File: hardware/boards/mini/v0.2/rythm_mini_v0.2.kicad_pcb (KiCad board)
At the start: 8 copper layers, 18 x 50 mm, 80 parts, among them IC1 NAU88C22YG, IC2 IS42S32160F-6BLI, Q1 PMV37EN22, U1 W25Q128JVP, U2 LTV-217-G, U4 STM32H750XBHx, U5 MT48LC32M8A2TG, Y1 Crystal_GND24

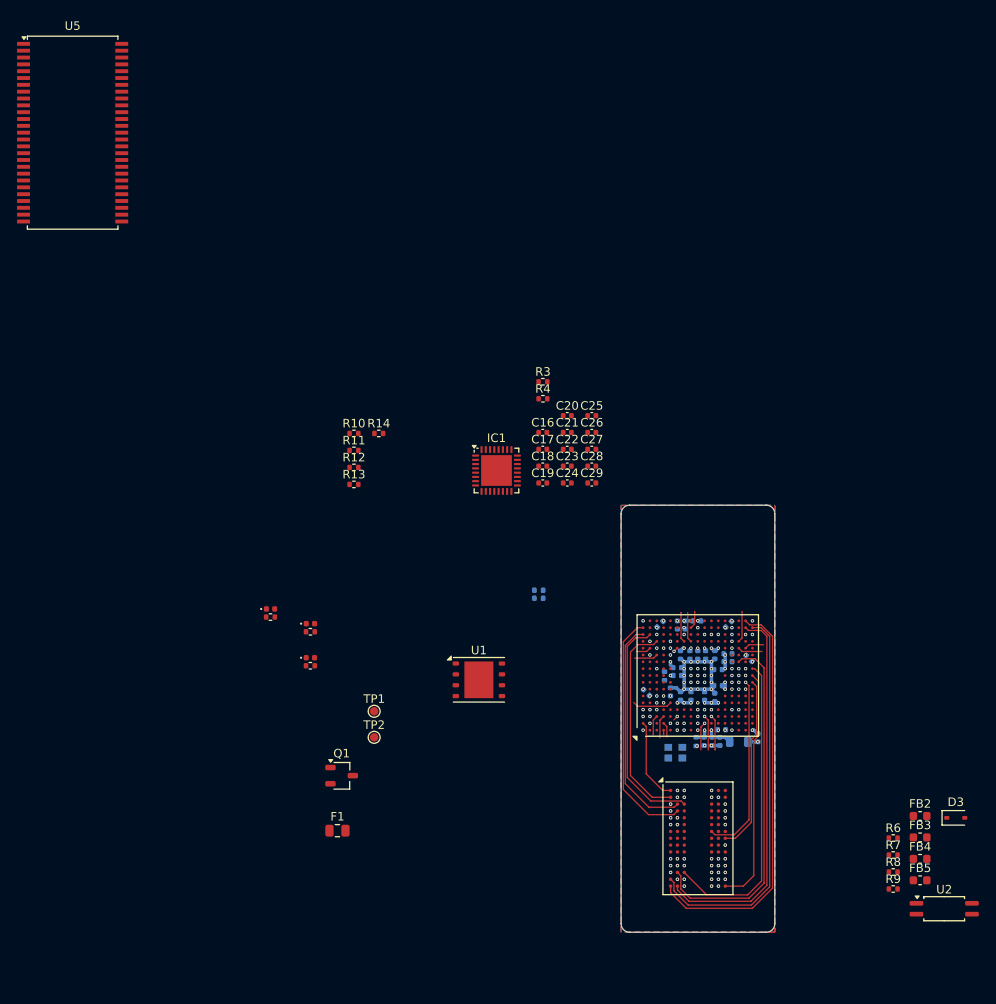
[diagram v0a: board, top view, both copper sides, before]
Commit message: minor module routing cleanup
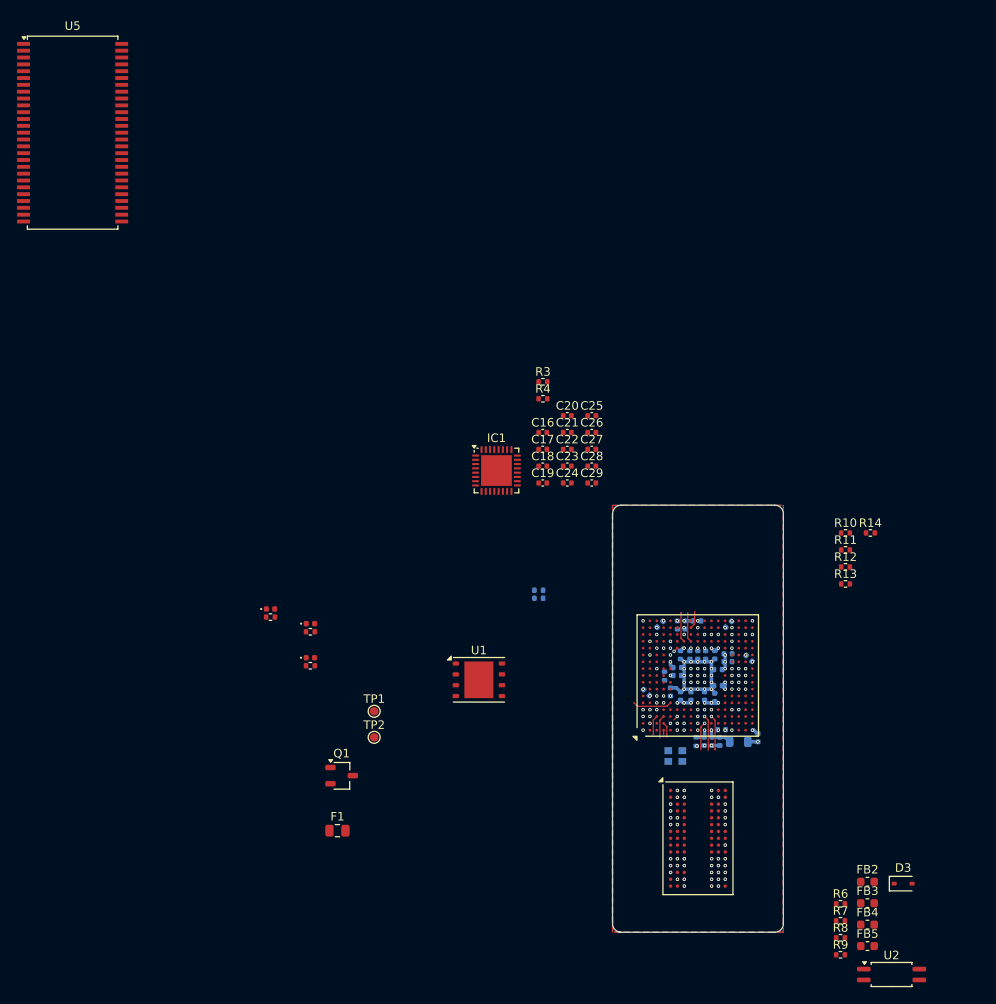
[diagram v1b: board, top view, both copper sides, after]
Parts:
- moved R10 58.7 mm to (97.3, 58.2)
- moved R11 58.7 mm to (97.3, 60.2)
- moved R12 58.7 mm to (97.3, 62.2)
- moved R13 58.7 mm to (97.3, 64.2)
- moved R14 58.7 mm to (100.2, 58.2)
- moved D3 9.86 mm to (104.0, 99.3)
- moved FB2 9.86 mm to (99.8, 99.1)
- moved FB4 9.86 mm to (99.8, 104.1)
- moved FB5 9.86 mm to (99.8, 106.6)
- moved R6 9.86 mm to (96.7, 101.7)
- moved R7 9.86 mm to (96.7, 103.7)
- moved R8 9.86 mm to (96.7, 105.7)
- moved R9 9.86 mm to (96.7, 107.6)
- moved U2 9.86 mm to (102.7, 110.0)
- moved FB3 9.86 mm to (99.8, 101.6)
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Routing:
- net /FMC_D14: track 47.8 -> 0.00 mm
- net /FMC_D13: track 46.1 -> 0.00 mm
- net /FMC_D15: track 44.3 -> 0.00 mm
- net /FMC_D12: track 41.8 -> 0.00 mm
- net /FMC_D0: track 38.5 -> 0.00 mm
- net /FMC_D1: track 38.2 -> 0.00 mm
- net /FMC_D11: track 36.3 -> 0.00 mm
- net /FMC_D5: track 28.5 -> 0.00 mm
- net /FMC_D24: track 28.0 -> 0.00 mm
- net /FMC_D4: track 27.8 -> 0.00 mm
- net /FMC_D26: track 26.6 -> 0.00 mm
- net /FMC_D25: track 26.2 -> 0.00 mm
- net /FMC_D27: track 23.8 -> 0.00 mm
- net /FMC_A10: track 21.5 -> 0.00 mm
- net /FMC_A11: track 20.7 -> 0.00 mm
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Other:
- board size 18 x 50 mm -> 20 x 50 mm

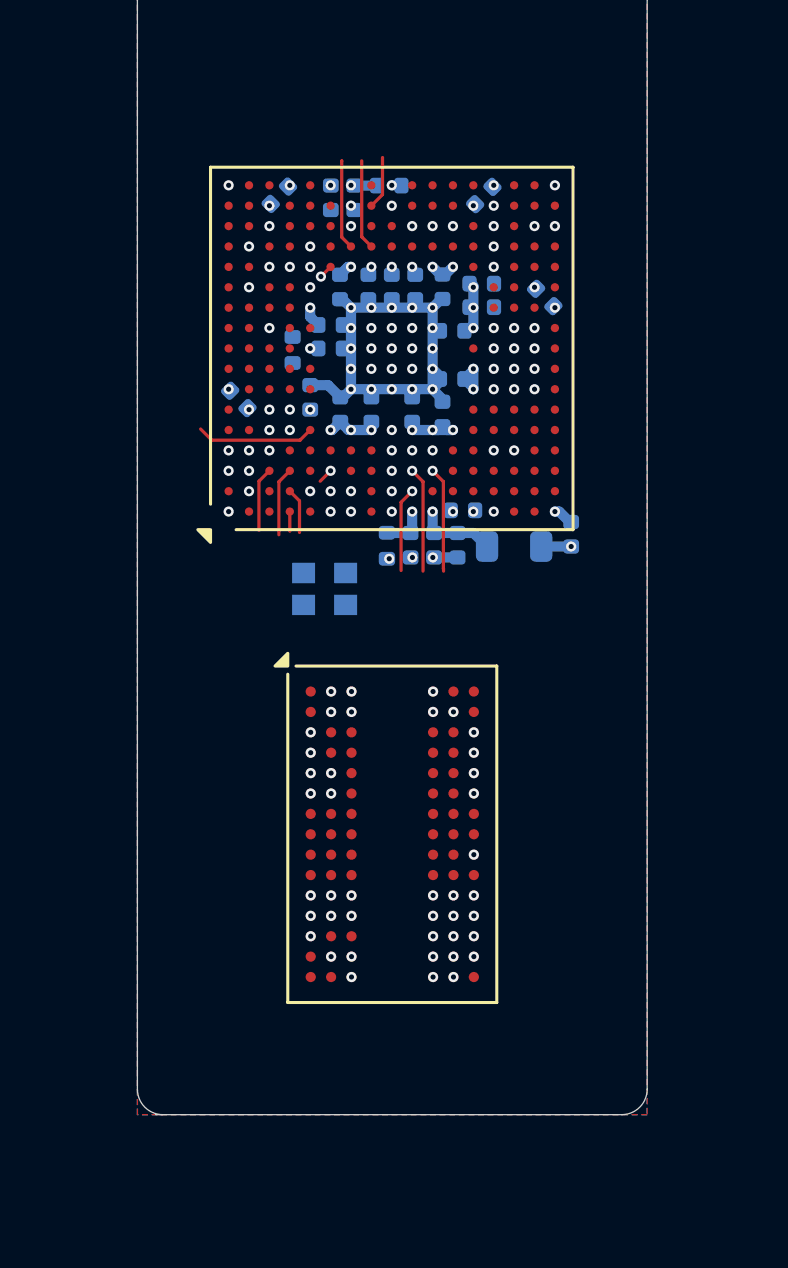
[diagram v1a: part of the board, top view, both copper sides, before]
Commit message: mini: test routing of x32 as x16
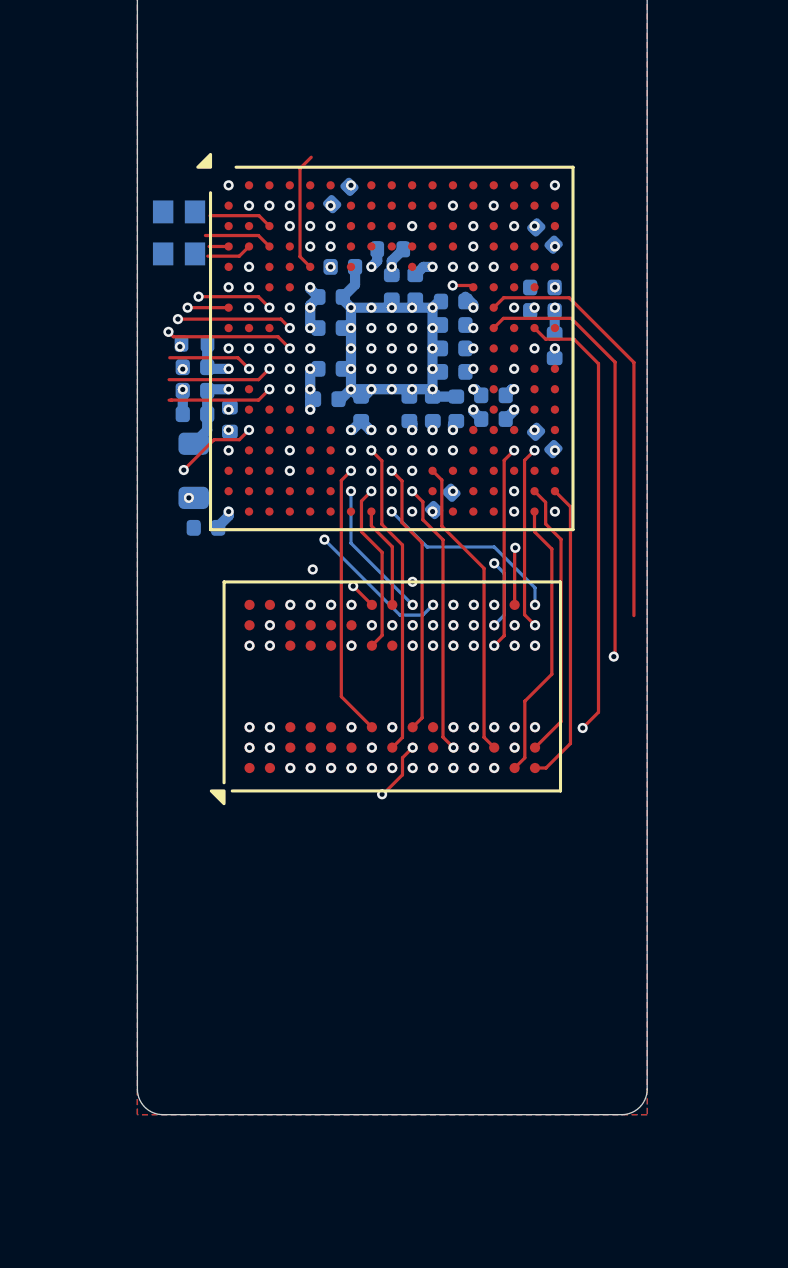
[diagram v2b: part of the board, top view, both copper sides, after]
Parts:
- added C7: 100nF, Capacitor_SMD:C_0402_1005Metric, B.Cu at (84.0, 76.8)
- moved Y1 15.1 mm to (71.6, 70.4), turned to 0 degrees
- moved C32 14.3 mm to (72.7, 82.0), turned to 0 degrees
- moved FB1 12.9 mm to (72.2, 79.7), turned to -90 degrees
- moved C31 11.5 mm to (72.3, 77.5), turned to 180 degrees
- moved C30 11.2 mm to (72.3, 76.6), turned to 180 degrees
- moved C33 11.0 mm to (72.3, 75.7), turned to 180 degrees
- moved R5 10.9 mm to (72.2, 74.8), turned to 0 degrees
- moved C2 10.5 mm to (86.0, 70.5), turned to 135 degrees
- moved C60 9.90 mm to (86.0, 78.5), turned to 135 degrees
- moved C15 9.81 mm to (73.6, 77.7), turned to -90 degrees
- moved C6 9.04 mm to (86.4, 74.8), turned to -90 degrees
- moved C4 9.02 mm to (85.9, 72.5), turned to 180 degrees
- moved C1 8.94 mm to (82.0, 80.9), turned to 45 degrees
- moved C3 8.94 mm to (78.0, 68.9), turned to -135 degrees
- moved C5 8.61 mm to (85.9, 73.5), turned to 180 degrees
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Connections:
- IC2 pad A1: /FMC_D28 -> unconnected-(IC2-DQ26-PadA1)
- IC2 pad A2: /FMC_D29 -> unconnected-(IC2-DQ24-PadA2)
- IC2 pad A8: /FMC_D21 -> unconnected-(IC2-DQ23-PadA8)
- IC2 pad A9: /FMC_D23 -> unconnected-(IC2-DQ21-PadA9)
- IC2 pad B1: /FMC_D27 -> unconnected-(IC2-DQ28-PadB1)
- IC2 pad B9: /FMC_D19 -> unconnected-(IC2-DQ19-PadB9)
- IC2 pad C2: /FMC_D25 -> unconnected-(IC2-DQ27-PadC2)
- IC2 pad C3: /FMC_D26 -> unconnected-(IC2-DQ25-PadC3)
- IC2 pad C7: /FMC_D22 -> unconnected-(IC2-DQ22-PadC7)
- IC2 pad C8: /FMC_D20 -> unconnected-(IC2-DQ20-PadC8)
- IC2 pad D2: /FMC_D24 -> unconnected-(IC2-DQ29-PadD2)
- IC2 pad D3: /FMC_D31 -> unconnected-(IC2-DQ30-PadD3)
- IC2 pad D7: /FMC_D17 -> unconnected-(IC2-DQ17-PadD7)
- IC2 pad D8: /FMC_D18 -> unconnected-(IC2-DQ18-PadD8)
- IC2 pad E2: /FMC_D30 -> unconnected-(IC2-DQ31-PadE2)
- IC2 pad E8: /FMC_D16 -> unconnected-(IC2-DQ16-PadE8)
- IC2 pad F2: /FMC_NBL3 -> unconnected-(IC2-DQM3-PadF2)
- IC2 pad F8: /FMC_NBL2 -> unconnected-(IC2-DQM2-PadF8)
- IC2 pad L2: /FMC_D8 -> /FMC_D10
- IC2 pad L8: /FMC_D7 -> /FMC_D5
- IC2 pad M2: /FMC_D10 -> /FMC_D9
- IC2 pad M3: /FMC_D9 -> /FMC_D11
- IC2 pad M8: /FMC_D5 -> /FMC_D7
- IC2 pad N3: /FMC_D11 -> /FMC_D8
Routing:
- net /FMC_CLK: track 0.00 -> 33.7 mm, vias 1 -> 2
- net /FMC_NBL1: track 0.00 -> 31.8 mm, vias 1 -> 2
- net /FMC_A3: track 0.00 -> 25.6 mm, vias 0 -> 3
- net /FMC_SDCKE0: track 0.00 -> 24.6 mm, vias 0 -> 4
- net /FMC_A12: track 2.06 -> 25.4 mm, vias 0 -> 2
- net /FMC_A5: track 4.78 -> 27.7 mm, vias 1 -> 3
- net /FMC_BA0: track 3.52 -> 25.3 mm, vias 0 -> 2
- net /FMC_A2: track 0.00 -> 21.2 mm, vias 1 -> 2
- net /FMC_A1: track 0.00 -> 20.2 mm, vias 0 -> 4
- net /FMC_NBL0: track 0.00 -> 18.5 mm, vias 1 -> 3
- net /FMC_D3: track 0.00 -> 15.1 mm, vias 2 -> 3
- net /FMC_D2: track 0.00 -> 14.8 mm
- net /FMC_A0: track 0.00 -> 14.5 mm, vias 0 -> 2
- net /FMC_NE1: track 0.54 -> 14.8 mm, vias 1 -> 2
- net /FMC_A7: track 0.00 -> 13.1 mm, vias 1 -> 2
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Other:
- outline, holes or cut-outs redrawn
